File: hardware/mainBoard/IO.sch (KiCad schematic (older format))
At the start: 15 parts

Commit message: Added the power part of the schematic
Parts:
- U? (x4): symbol chinaland:MC3403 -> prockeckv2-rescue:MC3403-chinaland
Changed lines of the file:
@@
 EESchema Schematic File Version 4
-LIBS:prockeckv2-cache
-LIBS:forcenOne-cache
-EELAYER 26 0
+EELAYER 30 0
 EELAYER END
 $Descr A4 11693 8268
@@
 Acondicionamiento diferencial
 $Comp
-L chinaland:MC3403 U?
+L prockeckv2-rescue:MC3403-chinaland U?
 U 1 1 5E701B88
 P 13250 5050
@@
 	12750 5400 13850 5400
 $Comp
-L chinaland:MC3403 U?
+L prockeckv2-rescue:MC3403-chinaland U?
 U 2 1 5E701B94
 P 13250 4200
@@
 Connection ~ 13850 5050
 $Comp
-L chinaland:MC3403 U?
+L prockeckv2-rescue:MC3403-chinaland U?
 U 3 1 5E701BA1
 P 14900 4900
@@
 	15050 4200 15100 4200
 $Comp
-L chinaland:MC3403 U?
+L prockeckv2-rescue:MC3403-chinaland U?
 U 5 1 5E701BB8
 P 15450 3850

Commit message: Added external connections, analog conditioning and several items
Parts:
- removed J?: O_Block1, symbol Connector:Screw_Terminal_01x20
- removed J?: O_Block2, symbol Connector:Screw_Terminal_01x20
- removed J?: I_Block1, symbol Connector:Screw_Terminal_01x14
- removed J?: I_Block2, symbol Connector:Screw_Terminal_01x14
- removed J?: ADC_Block1, symbol Connector:Screw_Terminal_01x12
- removed J?: ADC_Block2, symbol Connector:Screw_Terminal_01x12
- removed R? (x2): 200k, Resistor_SMD:R_0603_1608Metric_Pad1.05x0.95mm_HandSolder, symbol Device:R
- removed R? (x3): 100k, Resistor_SMD:R_0603_1608Metric_Pad1.05x0.95mm_HandSolder, symbol Device:R
- removed U? (x4): MC3403, Package_SO:SOIC-14_3.9x8.7mm_P1.27mm, symbol prockeckv2-rescue:MC3403-chinaland
- added J?: Screw_Terminal_01x20, symbol Connector:Screw_Terminal_01x20
- added J?: Screw_Terminal_01x01, symbol Connector:Screw_Terminal_01x01
- added J?: Screw_Terminal_01x06, symbol Connector:Screw_Terminal_01x06
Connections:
- net labels added: DAC, IO1, IO1_1, IO1_10, IO1_11, IO1_12, IO1_13, IO1_14, IO1_15, IO1_2, IO1_3, IO1_4, IO1_5, IO1_6, IO1_7, IO1_8, IO1_9, PWM, PWM1, PWM2, PWM3, PWM4
- net labels removed: +5V, -5V, ADC1_1, ADC1_2, ADC2_1, ADC2_2, ADC3_1, ADC3_2, ADC4_1, ADC4_2, ADC5_1, ADC5_2, ADC6_1, ADC6_2, ADC_INPUTS, ADCs, DI1_1, DI1_2, DI2_1, DI2_2, DI3_1, DI3_2, DI4_1, DI4_2, DI5_1, DI5_2, DI6_1, DI6_2, DI7_1, DI7_2, DO10_1, DO10_2, DO1_1, DO1_2, DO2_1, DO2_2, DO3_1, DO3_2, DO4_1, DO4_2, DO5_1, DO5_2, DO6_1, DO6_2, DO7_1, DO7_2, DO8_1, DO8_2, DO9_1, DO9_2, D_INPUTS, D_INS, D_OUTPUTS, D_OUTS, LVDT, LVDT+, LVDT-
- wire segments 169 -> 36
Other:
- note removed: "Acondicionamiento diferencial"

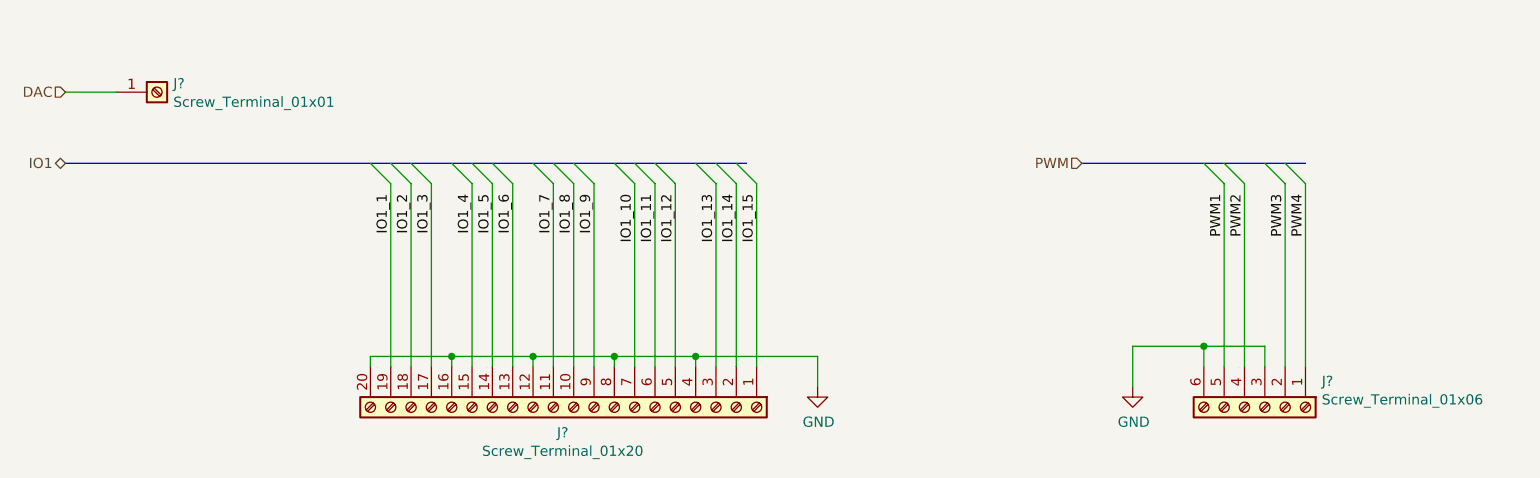
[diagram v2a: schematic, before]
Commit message: Ended schematic, created some pcb footprints
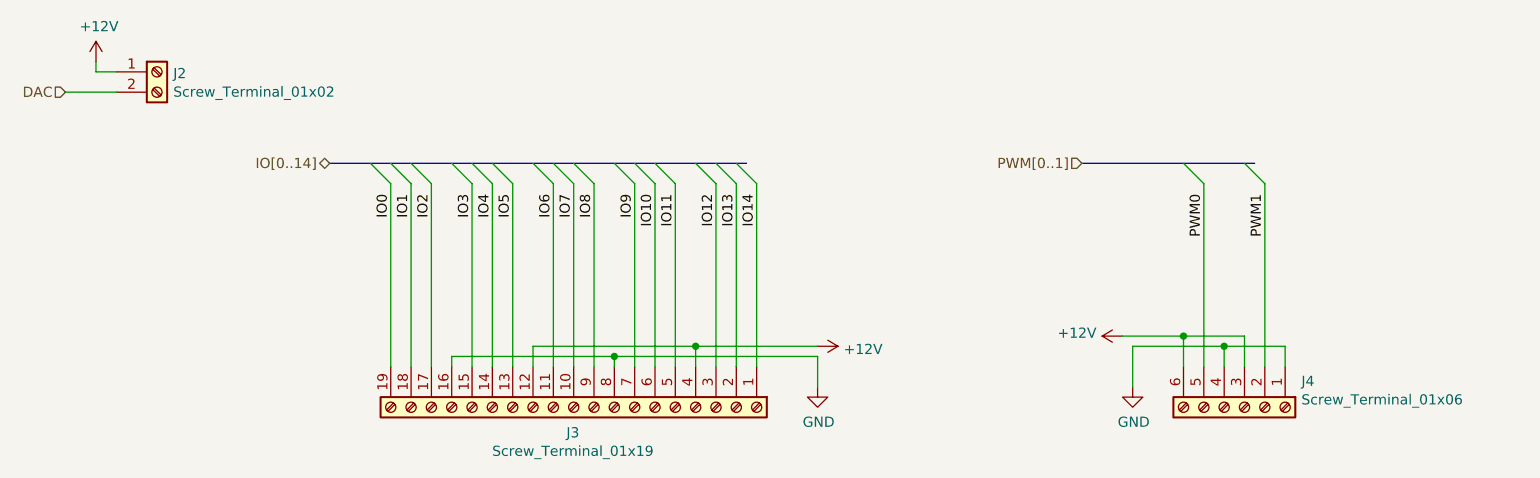
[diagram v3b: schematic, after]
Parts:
- removed J?: Screw_Terminal_01x20, symbol Connector:Screw_Terminal_01x20
- removed J?: Screw_Terminal_01x01, symbol Connector:Screw_Terminal_01x01
- added J2: Screw_Terminal_01x02, TerminalBlock:TerminalBlock_bornier-2_P5.08mm, symbol Connector:Screw_Terminal_01x02
- added J3: Screw_Terminal_01x19, chinalandfoot:TerminalBlock_19_P5.08mm, symbol Connector:Screw_Terminal_01x19
- J4: renamed from J?; footprint (none) -> TerminalBlock:TerminalBlock_bornier-6_P5.08mm
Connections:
- net PWM2 is gone; now on net GND: J4.4 (Pin_4)
- net PWM3 is gone; now on net PWM1: J4.2 (Pin_2)
- net PWM4 is gone; now on net GND: J4.1 (Pin_1)
- net DAC: now also J2.2 (Pin_2)
- net GND: now also J3.16 (Pin_16), J3.8 (Pin_8); no longer J4.3 (Pin_3), J4.6 (Pin_6)
- net IO1: now also J3.18 (Pin_18)
- net PWM1: no longer J4.5 (Pin_5)
- new net +12V: J2.1 (Pin_1), J3.12 (Pin_12), J3.4 (Pin_4), J4.3 (Pin_3), J4.6 (Pin_6)
- new net IO0: J3.19 (Pin_19)
- new net IO10: J3.6 (Pin_6)
- new net IO11: J3.5 (Pin_5)
- new net IO12: J3.3 (Pin_3)
- new net IO13: J3.2 (Pin_2)
- new net IO14: J3.1 (Pin_1)
- new net IO2: J3.17 (Pin_17)
- new net IO3: J3.15 (Pin_15)
- new net IO4: J3.14 (Pin_14)
- new net IO5: J3.13 (Pin_13)
- new net IO6: J3.11 (Pin_11)
- new net IO7: J3.10 (Pin_10)
- new net IO8: J3.9 (Pin_9)
- new net IO9: J3.7 (Pin_7)
- new net PWM0: J4.5 (Pin_5)
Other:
- moved on the sheet: J4
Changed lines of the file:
@@
 $Descr A4 11693 8268
 encoding utf-8
-Sheet 2 8
+Sheet 2 10
 Title ""
 Date ""
@@
 Comment4 ""
 $EndDescr
-$Comp
-L Connector:Screw_Terminal_01x20 J?
-U 1 1 5E51841F
-P 4500 3650
-F 0 "J?" V 4625 3596 50  0000 C CNN
-F 1 "Screw_Terminal_01x20" V 4716 3596 50  0000 C CNN
-F 2 "" H 4500 3650 50  0001 C CNN
-F 3 "~" H 4500 3650 50  0001 C CNN
-	1    4500 3650
-	0    1    1    0
-$EndComp
-Text HLabel 2000 2450 0    50   BiDi ~ 0
-IO1
-Wire Wire Line
-	3600 3450 3600 2550
-Wire Wire Line
-	3700 2550 3700 3450
-Wire Wire Line
-	3800 2550 3800 3450
-Wire Wire Line
-	4000 3450 4000 2550
-Wire Wire Line
-	4100 2550 4100 3450
-Wire Wire Line
-	4200 3450 4200 2550
-Wire Wire Line
-	4400 3450 4400 2550
-Wire Wire Line
-	4500 2550 4500 3450
-Wire Wire Line
-	4600 2550 4600 3450
-Wire Wire Line
-	4800 3450 4800 2550
-Wire Wire Line
-	4900 2550 4900 3450
-Wire Wire Line
-	5000 3450 5000 2550
-Wire Wire Line
-	5200 3450 5200 2550
-Wire Wire Line
-	5300 2550 5300 3450
-Wire Wire Line
-	5400 3450 5400 2550
-$Comp
-L power:GND #PWR?
+Text HLabel 3300 2450 0    50   BiDi ~ 0
+IO[0..14]
+$Comp
+L power:GND #PWR04
 U 1 1 5E5225D5
 P 5700 3550
-F 0 "#PWR?" H 5700 3300 50  0001 C CNN
+F 0 "#PWR04" H 5700 3300 50  0001 C CNN
 F 1 "GND" H 5705 3377 50  0000 C CNN
 F 2 "" H 5700 3550 50  0001 C CNN
@@
 	1    0    0    -1
 $EndComp
-Wire Wire Line
-	5700 3550 5700 3400
-Wire Wire Line
-	5700 3400 5100 3400
-Wire Wire Line
-	5100 3400 5100 3450
-Wire Wire Line
-	5100 3400 4700 3400
-Wire Wire Line
-	4700 3400 4700 3450
-Connection ~ 5100 3400
-Wire Wire Line
-	4700 3400 4300 3400
-Wire Wire Line
-	4300 3400 4300 3450
-Connection ~ 4700 3400
-Wire Wire Line
-	4300 3400 3900 3400
-Wire Wire Line
-	3900 3400 3900 3450
-Connection ~ 4300 3400
-Wire Wire Line
-	3900 3400 3500 3400
-Wire Wire Line
-	3500 3400 3500 3450
-Connection ~ 3900 3400
 Entry Wire Line
 	3500 2450 3600 2550
@@
 	5300 2450 5400 2550
 Text Label 3600 2600 3    50   ~ 0
-IO1_1
+IO0
 Text Label 3700 2600 3    50   ~ 0
-IO1_2
+IO1
 Text Label 3800 2600 3    50   ~ 0
-IO1_3
+IO2
 Text Label 4000 2600 3    50   ~ 0
-IO1_4
+IO3
 Text Label 4100 2600 3    50   ~ 0
-IO1_5
+IO4
 Text Label 4200 2600 3    50   ~ 0
-IO1_6
+IO5
 Text Label 4400 2600 3    50   ~ 0
-IO1_7
+IO6
 Text Label 4500 2600 3    50   ~ 0
-IO1_8
+IO7
 Text Label 4600 2600 3    50   ~ 0
-IO1_9
+IO8
 Text Label 4800 2600 3    50   ~ 0
-IO1_10
+IO9
 Text Label 4900 2600 3    50   ~ 0
-IO1_11
+IO10
 Text Label 5000 2600 3    50   ~ 0
-IO1_12
+IO11
 Text Label 5200 2600 3    50   ~ 0
-IO1_13
+IO12
 Text Label 5400 2600 3    50   ~ 0
-IO1_15
+IO14
 Text Label 5300 2600 3    50   ~ 0
-IO1_14
-$Comp
-L Connector:Screw_Terminal_01x01 J?
-U 1 1 5E56C93B
-P 2450 2100
-F 0 "J?" H 2530 2142 50  0000 L CNN
-F 1 "Screw_Terminal_01x01" H 2530 2051 50  0000 L CNN
-F 2 "" H 2450 2100 50  0001 C CNN
-F 3 "~" H 2450 2100 50  0001 C CNN
-	1    2450 2100
-	1    0    0    -1
-$EndComp
+IO13
 Text HLabel 2000 2100 0    50   Input ~ 0
 DAC
-Wire Wire Line
-	2000 2100 2250 2100
-$Comp
-L Connector:Screw_Terminal_01x06 J?
-U 1 1 5E57511A
-P 7900 3650
-F 0 "J?" V 7772 3930 50  0000 L CNN
-F 1 "Screw_Terminal_01x06" V 7863 3930 50  0000 L CNN
-F 2 "" H 7900 3650 50  0001 C CNN
-F 3 "~" H 7900 3650 50  0001 C CNN
-	1    7900 3650
-	0    1    1    0
-$EndComp
 Text HLabel 7000 2450 0    50   Input ~ 0
-PWM
-Wire Bus Line
-	7000 2450 8100 2450
-$Comp
-L power:GND #PWR?
+PWM[0..1]
+$Comp
+L power:GND #PWR06
 U 1 1 5E57A347
 P 7250 3550
-F 0 "#PWR?" H 7250 3300 50  0001 C CNN
+F 0 "#PWR06" H 7250 3300 50  0001 C CNN
 F 1 "GND" H 7255 3377 50  0000 C CNN
 F 2 "" H 7250 3550 50  0001 C CNN
@@
 	1    0    0    -1
 $EndComp
+Entry Wire Line
+	7500 2450 7600 2550
+Entry Wire Line
+	7800 2450 7900 2550
+Text Label 7600 2600 3    50   ~ 0
+PWM0
+Text Label 7900 2600 3    50   ~ 0
+PWM1
+$Comp
+L Connector:Screw_Terminal_01x06 J4
+U 1 1 5E57511A
+P 7800 3650
+F 0 "J4" V 7672 3930 50  0000 L CNN
+F 1 "Screw_Terminal_01x06" V 7763 3930 50  0000 L CNN
+F 2 "TerminalBlock:TerminalBlock_bornier-6_P5.08mm" H 7800 3650 50  0001 C CNN
+F 3 "~" H 7800 3650 50  0001 C CNN
+	1    7800 3650
+	0    1    1    0
+$EndComp
+$Comp
+L Connector:Screw_Terminal_01x02 J2
+U 1 1 5E07BAAA
+P 2450 2000
+F 0 "J2" H 2530 1992 50  0000 L CNN
+F 1 "Screw_Terminal_01x02" H 2530 1901 50  0000 L CNN
+F 2 "TerminalBlock:TerminalBlock_bornier-2_P5.08mm" H 2450 2000 50  0001 C CNN
+F 3 "~" H 2450 2000 50  0001 C CNN
+	1    2450 2000
+	1    0    0    -1
+$EndComp
+$Comp
+L power:+12V #PWR02
+U 1 1 5E07BFC3
+P 2150 1950
+F 0 "#PWR02" H 2150 1800 50  0001 C CNN
+F 1 "+12V" H 2165 2123 50  0000 C CNN
+F 2 "" H 2150 1950 50  0001 C CNN
+F 3 "" H 2150 1950 50  0001 C CNN
+	1    2150 1950
+	1    0    0    -1
+$EndComp
+$Comp
+L power:+12V #PWR03
+U 1 1 5E0C9166
+P 5700 3350
+F 0 "#PWR03" H 5700 3200 50  0001 C CNN
+F 1 "+12V" V 5715 3478 50  0000 L CNN
+F 2 "" H 5700 3350 50  0001 C CNN
+F 3 "" H 5700 3350 50  0001 C CNN
+	1    5700 3350
+	0    1    1    0
+$EndComp
+$Comp
+L power:+12V #PWR05
+U 1 1 5E0D82DA
+P 7200 3300
+F 0 "#PWR05" H 7200 3150 50  0001 C CNN
+F 1 "+12V" V 7215 3428 50  0000 L CNN
+F 2 "" H 7200 3300 50  0001 C CNN
+F 3 "" H 7200 3300 50  0001 C CNN
+	1    7200 3300
+	0    -1   -1   0
+$EndComp
+Wire Wire Line
+	3600 3450 3600 2550
+Wire Wire Line
+	3700 2550 3700 3450
+Wire Wire Line
+	3800 2550 3800 3450
+Wire Wire Line
+	4000 3450 4000 2550
+Wire Wire Line
+	4100 2550 4100 3450
+Wire Wire Line
+	4200 3450 4200 2550
+Wire Wire Line
+	4400 3450 4400 2550
+Wire Wire Line
+	4500 2550 4500 3450
+Wire Wire Line
+	4600 2550 4600 3450
+Wire Wire Line
+	4800 3450 4800 2550
+Wire Wire Line
+	4900 2550 4900 3450
+Wire Wire Line
+	5200 3450 5200 2550
+Wire Wire Line
+	5300 2550 5300 3450
+Wire Wire Line
+	5400 3450 5400 2550
+Wire Wire Line
+	5700 3550 5700 3400
+Wire Wire Line
+	4700 3400 4700 3450
+Connection ~ 4700 3400
+Wire Wire Line
+	3900 3400 3900 3450
+Wire Wire Line
+	2000 2100 2250 2100
 Wire Wire Line
 	7250 3550 7250 3350
 Wire Wire Line
-	7250 3350 7600 3350
-Wire Wire Line
-	7600 3350 7600 3450
-Wire Wire Line
-	7600 3350 7900 3350
-Wire Wire Line
-	7900 3350 7900 3450
-Connection ~ 7600 3350
-Wire Wire Line
-	7700 3450 7700 2550
-Wire Wire Line
-	7800 3450 7800 2550
-Wire Wire Line
-	8000 3450 8000 2550
-Wire Wire Line
-	8100 3450 8100 2550
+	7600 3450 7600 2550
+Wire Wire Line
+	7900 3450 7900 2550
+Wire Wire Line
+	7700 3350 7700 3450
+Wire Wire Line
+	2150 1950 2150 2000
+Wire Wire Line
+	2150 2000 2250 2000
+Wire Wire Line
+	3900 3400 4700 3400
+Wire Wire Line
+	4700 3400 5700 3400
+Wire Wire Line
+	5700 3350 5100 3350
+Wire Wire Line
+	5100 3350 5100 3450
+Wire Wire Line
+	5000 3450 5000 2550
+Wire Wire Line
+	5100 3350 4300 3350
+Wire Wire Line
+	4300 3350 4300 3450
+Connection ~ 5100 3350
+Wire Wire Line
+	7250 3350 7700 3350
+Wire Wire Line
+	7200 3300 7500 3300
+Wire Wire Line
+	7500 3300 7500 3450
+Wire Wire Line
+	7500 3300 7800 3300
+Wire Wire Line
+	7800 3300 7800 3450
+Connection ~ 7500 3300
+Wire Wire Line
+	8000 3450 8000 3350
+Wire Wire Line
+	8000 3350 7700 3350
+Connection ~ 7700 3350
 Wire Bus Line
-	2000 2450 5350 2450
-Entry Wire Line
-	7600 2450 7700 2550
-Entry Wire Line
-	7700 2450 7800 2550
-Entry Wire Line
-	7900 2450 8000 2550
-Entry Wire Line
-	8000 2450 8100 2550
-Text Label 7700 2600 3    50   ~ 0
-PWM1
-Text Label 7800 2600 3    50   ~ 0
-PWM2
-Text Label 8000 2600 3    50   ~ 0
-PWM3
-Text Label 8100 2600 3    50   ~ 0
-PWM4
+	7000 2450 7850 2450
+Wire Bus Line
+	3300 2450 5350 2450
+$Comp
+L Connector:Screw_Terminal_01x19 J3
+U 1 1 5DF27906
+P 4500 3650
+F 0 "J3" V 4625 3646 50  0000 C CNN
+F 1 "Screw_Terminal_01x19" V 4716 3646 50  0000 C CNN
+F 2 "chinalandfoot:TerminalBlock_19_P5.08mm" H 4500 3650 50  0001 C CNN
+F 3 "~" H 4500 3650 50  0001 C CNN
+	1    4500 3650
+	0    1    1    0
+$EndComp
 $EndSCHEMATC

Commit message: First working software
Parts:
- J2: footprint TerminalBlock:TerminalBlock_bornier-2_P5.08mm -> Connector_PinHeader_2.54mm:PinHeader_1x02_P2.54mm_Vertical
- J4: footprint TerminalBlock:TerminalBlock_bornier-6_P5.08mm -> Connector_PinHeader_2.54mm:PinHeader_1x06_P2.54mm_Vertical
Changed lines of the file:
@@
 EESchema Schematic File Version 4
+LIBS:prockeckv2-cache
 EELAYER 30 0
 EELAYER END
@@
 F 0 "J4" V 7672 3930 50  0000 L CNN
 F 1 "Screw_Terminal_01x06" V 7763 3930 50  0000 L CNN
-F 2 "TerminalBlock:TerminalBlock_bornier-6_P5.08mm" H 7800 3650 50  0001 C CNN
+F 2 "Connector_PinHeader_2.54mm:PinHeader_1x06_P2.54mm_Vertical" H 7800 3650 50  0001 C CNN
 F 3 "~" H 7800 3650 50  0001 C CNN
 	1    7800 3650
@@
 F 0 "J2" H 2530 1992 50  0000 L CNN
 F 1 "Screw_Terminal_01x02" H 2530 1901 50  0000 L CNN
-F 2 "TerminalBlock:TerminalBlock_bornier-2_P5.08mm" H 2450 2000 50  0001 C CNN
+F 2 "Connector_PinHeader_2.54mm:PinHeader_1x02_P2.54mm_Vertical" H 2450 2000 50  0001 C CNN
 F 3 "~" H 2450 2000 50  0001 C CNN
 	1    2450 2000
